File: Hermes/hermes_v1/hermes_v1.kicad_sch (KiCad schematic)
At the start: 25 parts, among them P1 ESC1_VCC, P2 ESC1_GND, P3 LIPO_VCC, P4 LIPO_GND, P5 ESC2_VCC, P6 ESC2_GND, U1 TPS5430DDAR, U2 LD1117S33TR_SOT223

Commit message: Hermes v2
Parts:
- removed H1, H2, H3, H4: MountingHole, MountingHole:MountingHole_2.2mm_M2_DIN965_Pad, symbol Mechanical:MountingHole
- removed JP1: SolderJumper_3_Bridged12, Jumper:SolderJumper-3_P1.3mm_Bridged12_RoundedPad1.0x1.5mm_NumberLabels, symbol Jumper:SolderJumper_3_Bridged12
- removed TP1: GND_BAT_Probe, TestPoint:TestPoint_Pad_D1.0mm, symbol Connector:TestPoint_Probe
- removed TP2: 5V_BAT_Probe, TestPoint:TestPoint_Pad_D1.0mm, symbol Connector:TestPoint_Probe
- added JP1: SolderJumper_3_Open, Jumper:SolderJumper-3_P1.3mm_Open_RoundedPad1.0x1.5mm_NumberLabels, symbol Jumper:SolderJumper_3_Open
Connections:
- net +5V: now also JP1.3 (B)
- net FC_USB_VBUS: now also JP1.1 (A)
- net REG_5VIN: now also JP1.2 (C)

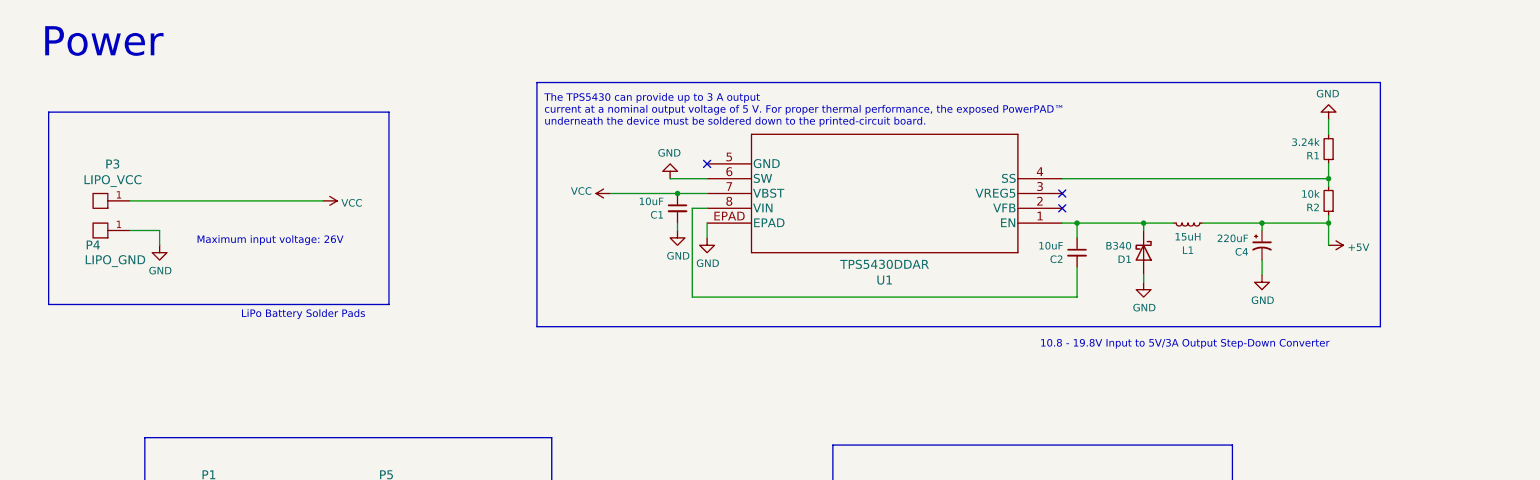
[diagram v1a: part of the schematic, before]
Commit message: Added VoltPak 1000
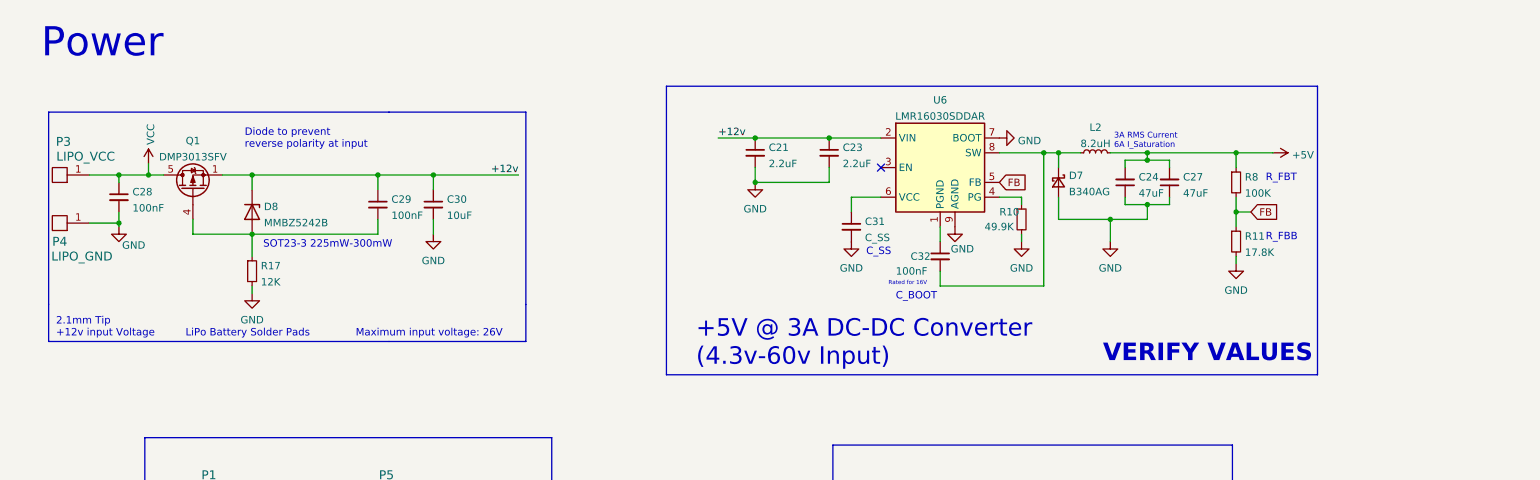
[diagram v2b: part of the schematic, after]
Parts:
- removed C1, C2: 10uF, Capacitor_SMD:C_0402_1005Metric_Pad0.74x0.62mm_HandSolder, symbol Device:C_Small
- removed C4: 220uF, Capacitor_SMD:CP_Elec_6.3x5.4, symbol Device:CP1_Small
- removed D1: B340, Diode_SMD:D_SMC, symbol Diode:B340
- removed L1: 15uH, Inductor_SMD:L_0402_1005Metric, symbol Device:L_Small
- removed R1: 3.24k, Resistor_SMD:R_0402_1005Metric_Pad0.72x0.64mm_HandSolder, symbol Device:R_Small
- removed R2: 10k, Resistor_SMD:R_0402_1005Metric_Pad0.72x0.64mm_HandSolder, symbol Device:R_Small
- removed U1: TPS5430DDAR, TPS5430DDAR:TPS5430DDAR, symbol TPS5430DDAR:TPS5430DDAR
- added C21, C23: 2.2uF, Capacitor_SMD:C_0402_1005Metric, symbol Device:C_Small
- added C24, C27: 47uF, Capacitor_SMD:C_0402_1005Metric, symbol Device:C_Small
- added C28, C29, C32: 100nF, Capacitor_SMD:C_0402_1005Metric, symbol Device:C_Small
- added C30: 10uF, Capacitor_SMD:C_0402_1005Metric, symbol Device:C_Small
- added C31: C_SS, Capacitor_SMD:C_0402_1005Metric, symbol Device:C_Small
- added D7: B340AG, Diode_SMD:D_SMB, symbol Device:D_Schottky_Small
- added D8: MMBZ5242B, Diode_SMD:D_SOT-23_ANK, symbol Diode:BZV55C12
- added L2: 8.2uH, Inductor_SMD:L_Bourns_SRP7028A_7.3x6.6mm, symbol Device:L_Small
- added Q1: DMP3013SFV, Package_SON:Diodes_PowerDI3333-8, symbol Transistor_FET:DMP3013SFV
- added R10: 49.9K, Resistor_SMD:R_0402_1005Metric, symbol Device:R_Small
- added R11: 17.8K, Resistor_SMD:R_0402_1005Metric, symbol Device:R_Small
- added R17: 12K, Resistor_SMD:R_0402_1005Metric, symbol Device:R_Small
- added R8: 100K, Resistor_SMD:R_0402_1005Metric, symbol Device:R_Small
- added U6: LMR16030SDDAR, Package_SO:Texas_HSOP-8-1EP_3.9x4.9mm_P1.27mm_ThermalVias, symbol Regulator_Switching:LMR33630ADDA
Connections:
- net +5V: now also C24.2, C27.2, L2.2, R8.1
- net GND: now also C21.2, C23.2, C24.1, C27.1, C28.2, C30.2, C31.2, D7.2 (A), R10.2, R11.2, R17.2, U6.7 (BOOT), U6.9 (AGND)
- net VCC: now also C28.1, Q1.5 (D)
- new net: C32.1, U6.1 (PGND)
- new net: C32.2, D7.1 (K), L2.1, U6.8 (SW)
- new net: C31.1, U6.6 (VCC)
- new net: C29.2, D8.2 (A), Q1.4 (G), R17.1
- new net: R10.1, U6.4 (PG)
- new net +12v: C21.1, C23.1, C29.1, C30.1, D8.1 (K), Q1.1 (S), Q1.2 (S), Q1.3 (S), U6.2 (VIN)
- new net FB: R11.1, R8.2, U6.5 (FB)
- no-connect marks 3 -> 1
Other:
- note added: "+5V @ 3A DC-DC Converter (4.3v-60v Input)"
- note added: "2.1mm Tip +12v input Voltage"
- note added: "3A RMS Current 6A I_Saturation"
- note added: "C_BOOT"
- note added: "C_SS"
- note added: "Diode to prevent reverse polarity at input"
- note added: "R_FBB"
- note added: "R_FBT"
- note added: "Rated for 16V"
- note added: "SOT23-3 225mW-300mW"
- note added: "VERIFY VALUES"
- note removed: "10.8 - 19.8V Input to 5V/3A Output Step-Down Converter"
- note removed: "The TPS5430 can provide up to 3 A output current at a nominal output voltage of 5 V. For proper thermal performance, the exposed PowerPAD™ underneath the device must be soldered down to the printed-circuit board."
- moved on the sheet: P3, P4
